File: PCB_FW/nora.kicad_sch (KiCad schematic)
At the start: 275 parts, among them J1 USB_C_Receptacle_USB2.0, J2 Conn_01x04, J3 Conn_01x02, J4 Conn_01x02, J5 Conn_02x03_Odd_Even, U1 ATmega32U4-MU, U2 24LC64, U4 Pico, Y1 16MHz

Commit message: PICOとREを接続 #89
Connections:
- net PICO_9 is gone; now on net RE1B_MOSI: J2.2 (Pin_2), U4.12 (GPIO9)
- net SCK is gone; now on net RE1A_SCK: J5.3 (Pin_3), RE_42.A, U1.9 (PB1)
- net row2: now also U4.27 (GPIO21); no longer U4.29 (GPIO22)
- net row7: now also U4.26 (GPIO20); no longer U4.27 (GPIO21)
- net MOSI renamed RE1B_MOSI
- net PICO_8 renamed RE1A_SCK
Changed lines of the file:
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@@
   (no_connect (at 358.775 62.865))
   (no_connect (at 528.32 57.785))
-  (no_connect (at 528.32 80.645))
+  (no_connect (at 528.32 73.025))
   (no_connect (at 344.17 236.22))
   (no_connect (at 528.32 70.485))
@@
     )
   )
-  (global_label "col0" (shape input) (at 492.76 52.705 180) (fields_autoplaced)
+  (global_label "RE1A_SCK" (shape input) (at 492.76 70.485 180) (fields_autoplaced)
     (effects (font (size 1.27 1.27)) (justify right))
-    (property "シート間のリファレンス" "${INTERSHEET_REFS}" (id 0) (at 0 0 0)
-      (effects (font (size 1.27 1.27)) hide)
+    (property "シート間のリファレンス" "${INTERSHEET_REFS}" (id 0) (at 481.0015 70.5644 0)
+      (effects (font (size 1.27 1.27)) (justify right) hide)
     )
   )
-  (global_label "SCK" (shape input) (at 328.295 172.72 180) (fields_autoplaced)
+  (global_label "col0" (shape input) (at 492.76 52.705 180) (fields_autoplaced)
     (effects (font (size 1.27 1.27)) (justify right))
     (property "シート間のリファレンス" "${INTERSHEET_REFS}" (id 0) (at 0 0 0)
@@
     )
   )
-  (global_label "PICO_9" (shape input) (at 492.76 73.025 180) (fields_autoplaced)
-    (effects (font (size 1.27 1.27)) (justify right))
-    (property "シート間のリファレンス" "${INTERSHEET_REFS}" (id 0) (at 0 0 0)
-      (effects (font (size 1.27 1.27)) hide)
-    )
-  )
   (global_label "Skip_R3RE" (shape input) (at 99.06 192.405 0) (fields_autoplaced)
     (effects (font (size 1.27 1.27)) (justify left))
@@
     )
   )
+  (global_label "RE1A_SCK" (shape input) (at 253.365 276.225 0) (fields_autoplaced)
+    (effects (font (size 1.27 1.27)) (justify left))
+    (property "シート間のリファレンス" "${INTERSHEET_REFS}" (id 0) (at 265.1235 276.1456 0)
+      (effects (font (size 1.27 1.27)) (justify left) hide)
+    )
+  )
   (global_label "RE1_S1" (shape input) (at 113.03 273.05 0) (fields_autoplaced)
     (effects (font (size 1.27 1.27)) (justify left))
@@
     )
   )
-  (global_label "row2" (shape input) (at 528.32 73.025 0) (fields_autoplaced)
+  (global_label "row2" (shape input) (at 528.32 78.105 0) (fields_autoplaced)
     (effects (font (size 1.27 1.27)) (justify left))
-    (property "シート間のリファレンス" "${INTERSHEET_REFS}" (id 0) (at 0 0 0)
+    (property "シート間のリファレンス" "${INTERSHEET_REFS}" (id 0) (at 0 5.08 0)
       (effects (font (size 1.27 1.27)) hide)
     )
   )
-  (global_label "PICO_8" (shape input) (at 253.365 276.225 0) (fields_autoplaced)
-    (effects (font (size 1.27 1.27)) (justify left))
-    (property "シート間のリファレンス" "${INTERSHEET_REFS}" (id 0) (at 0 0 0)
-      (effects (font (size 1.27 1.27)) hide)
+  (global_label "RE1B_MOSI" (shape input) (at 492.76 73.025 180) (fields_autoplaced)
+    (effects (font (size 1.27 1.27)) (justify right))
+    (property "シート間のリファレンス" "${INTERSHEET_REFS}" (id 0) (at 479.9734 73.1044 0)
+      (effects (font (size 1.27 1.27)) (justify right) hide)
     )
   )
@@
     )
   )
-  (global_label "MOSI" (shape input) (at 97.79 278.13 180) (fields_autoplaced)
+  (global_label "RE1B_MOSI" (shape input) (at 97.79 278.13 180) (fields_autoplaced)
     (effects (font (size 1.27 1.27)) (justify right))
-    (property "シート間のリファレンス" "${INTERSHEET_REFS}" (id 0) (at 487.045 330.835 0)
-      (effects (font (size 1.27 1.27)) hide)
+    (property "シート間のリファレンス" "${INTERSHEET_REFS}" (id 0) (at 85.0034 278.0506 0)
+      (effects (font (size 1.27 1.27)) (justify right) hide)
     )
   )
@@
     )
   )
-  (global_label "SCK" (shape input) (at 389.255 50.165 0) (fields_autoplaced)
+  (global_label "RE1A_SCK" (shape input) (at 389.255 50.165 0) (fields_autoplaced)
     (effects (font (size 1.27 1.27)) (justify left))
-    (property "シート間のリファレンス" "${INTERSHEET_REFS}" (id 0) (at 0 0 0)
-      (effects (font (size 1.27 1.27)) hide)
+    (property "シート間のリファレンス" "${INTERSHEET_REFS}" (id 0) (at 401.0135 50.0856 0)
+      (effects (font (size 1.27 1.27)) (justify left) hide)
     )
   )
@@
     )
   )
-  (global_label "MOSI" (shape input) (at 389.255 52.705 0) (fields_autoplaced)
+  (global_label "RE1B_MOSI" (shape input) (at 389.255 52.705 0) (fields_autoplaced)
     (effects (font (size 1.27 1.27)) (justify left))
-    (property "シート間のリファレンス" "${INTERSHEET_REFS}" (id 0) (at 0 0 0)
-      (effects (font (size 1.27 1.27)) hide)
+    (property "シート間のリファレンス" "${INTERSHEET_REFS}" (id 0) (at 402.0416 52.6256 0)
+      (effects (font (size 1.27 1.27)) (justify left) hide)
     )
   )
@@
     )
   )
-  (global_label "row7" (shape input) (at 528.32 78.105 0) (fields_autoplaced)
+  (global_label "row7" (shape input) (at 528.32 80.645 0) (fields_autoplaced)
     (effects (font (size 1.27 1.27)) (justify left))
-    (property "シート間のリファレンス" "${INTERSHEET_REFS}" (id 0) (at 0 0 0)
+    (property "シート間のリファレンス" "${INTERSHEET_REFS}" (id 0) (at 0 2.54 0)
       (effects (font (size 1.27 1.27)) hide)
     )
@@
     )
   )
-  (global_label "SCK" (shape input) (at 97.79 273.05 180) (fields_autoplaced)
+  (global_label "RE1A_SCK" (shape input) (at 97.79 273.05 180) (fields_autoplaced)
     (effects (font (size 1.27 1.27)) (justify right))
-    (property "シート間のリファレンス" "${INTERSHEET_REFS}" (id 0) (at 487.045 323.215 0)
-      (effects (font (size 1.27 1.27)) hide)
+    (property "シート間のリファレンス" "${INTERSHEET_REFS}" (id 0) (at 86.0315 272.9706 0)
+      (effects (font (size 1.27 1.27)) (justify right) hide)
     )
   )
@@
     )
   )
-  (global_label "PICO_9" (shape input) (at 253.365 273.685 0) (fields_autoplaced)
+  (global_label "RE1B_MOSI" (shape input) (at 340.995 172.72 0) (fields_autoplaced)
     (effects (font (size 1.27 1.27)) (justify left))
-    (property "シート間のリファレンス" "${INTERSHEET_REFS}" (id 0) (at 0 0 0)
-      (effects (font (size 1.27 1.27)) hide)
+    (property "シート間のリファレンス" "${INTERSHEET_REFS}" (id 0) (at 353.7816 172.6406 0)
+      (effects (font (size 1.27 1.27)) (justify left) hide)
     )
   )
@@
     )
   )
+  (global_label "RE1A_SCK" (shape input) (at 328.295 172.72 180) (fields_autoplaced)
+    (effects (font (size 1.27 1.27)) (justify right))
+    (property "シート間のリファレンス" "${INTERSHEET_REFS}" (id 0) (at 316.5365 172.7994 0)
+      (effects (font (size 1.27 1.27)) (justify right) hide)
+    )
+  )
   (global_label "row5" (shape input) (at 20.32 48.26 180) (fields_autoplaced)
     (effects (font (size 1.27 1.27)) (justify right))
@@
     )
   )
-  (global_label "PICO_8" (shape input) (at 492.76 70.485 180) (fields_autoplaced)
-    (effects (font (size 1.27 1.27)) (justify right))
-    (property "シート間のリファレンス" "${INTERSHEET_REFS}" (id 0) (at 0 0 0)
-      (effects (font (size 1.27 1.27)) hide)
-    )
-  )
   (global_label "col4" (shape input) (at 389.255 121.285 0) (fields_autoplaced)
     (effects (font (size 1.27 1.27)) (justify left))
@@
     )
   )
-  (global_label "MOSI" (shape input) (at 340.995 172.72 0) (fields_autoplaced)
-    (effects (font (size 1.27 1.27)) (justify left))
-    (property "シート間のリファレンス" "${INTERSHEET_REFS}" (id 0) (at 0 0 0)
-      (effects (font (size 1.27 1.27)) hide)
-    )
-  )
   (global_label "LED" (shape input) (at 528.32 60.325 0) (fields_autoplaced)
     (effects (font (size 1.27 1.27)) (justify left))
@@
     )
   )
+  (global_label "RE1B_MOSI" (shape input) (at 253.365 273.685 0) (fields_autoplaced)
+    (effects (font (size 1.27 1.27)) (justify left))
+    (property "シート間のリファレンス" "${INTERSHEET_REFS}" (id 0) (at 266.1516 273.6056 0)
+      (effects (font (size 1.27 1.27)) (justify left) hide)
+    )
+  )

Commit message: LEDの穴サイズを縦3.2→3.0mmに変更
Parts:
- L1, L10, L11, L12, L13, L14, L15, L16, L17, L18, L19, L2, L20, L21, L22, L23, L25, L26, L27, L28, L29, L3, L30, L31, L32, L33, L34, L35, L36, L37, L4, L41, L42, L43, L44, L45, L46, L47, L48, L49, L5, L50, L51, L52, L53, L56, L57, L58, L59, L6, L60, L61, L62, L63, L64, L65, L66, L68, L69, L7, L70, L71: footprint Jones.local:YS-SK6812MINI-E_large_hole_with_small_pad -> Jones.local:YS-SK6812MINI-E_middle_hole_with_small_pad
- L24, L38, L39, L40, L54, L55, L67, L8, L9: footprint Jones.local:YS-SK6812MINI-E_large_hole_with_small_pad_reserved -> Jones.local:YS-SK6812MINI-E_middle_hole_with_small_pad_reserved

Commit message: REとFWで異なるソケットの配置をわかりやすくした #109
最下段中央REのソケット
　斜線パターン
　RE→○
R3中央REのソケット
　クロスパターン
　RE→×
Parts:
- SW_37, SW_47: footprint Keebio-Parts:Kailh-PG1350-1u-MBK-WithKeyName-Socket-1.8mm-hole-reflection-half-paint -> Keebio-Parts:Kailh-PG1350-1u-MBK-WithKeyName-Socket-1.8mm-hole-reflection-cross-paint
- SW_44: footprint Keebio-Parts:Kailh-PG1350-1.5u-MBK-WithKeyName-Socket-1.8mm-hole-reflection-frame-only -> Keebio-Parts:Kailh-PG1350-1.5u-MBK-WithKeyName-Socket-1.8mm-hole-reflection-half-paint
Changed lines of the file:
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@@
     (property "Reference" "SW_37" (id 0) (at 145.415 74.041 0))
     (property "Value" ";:" (id 1) (at 145.415 76.3524 0))
-    (property "Footprint" "Keebio-Parts:Kailh-PG1350-1u-MBK-WithKeyName-Socket-1.8mm-hole-reflection-half-paint" (id 2) (at 145.415 76.2 0)
+    (property "Footprint" "Keebio-Parts:Kailh-PG1350-1u-MBK-WithKeyName-Socket-1.8mm-hole-reflection-cross-paint" (id 2) (at 145.415 76.2 0)
       (effects (font (size 1.27 1.27)) hide)
     )
@@
     (property "Reference" "SW_47" (id 0) (at 178.435 74.041 0))
     (property "Value" "'\"" (id 1) (at 178.435 76.3524 0))
-    (property "Footprint" "Keebio-Parts:Kailh-PG1350-1u-MBK-WithKeyName-Socket-1.8mm-hole-reflection-half-paint" (id 2) (at 178.435 76.2 0)
+    (property "Footprint" "Keebio-Parts:Kailh-PG1350-1u-MBK-WithKeyName-Socket-1.8mm-hole-reflection-cross-paint" (id 2) (at 178.435 76.2 0)
       (effects (font (size 1.27 1.27)) hide)
     )
@@
     (property "Reference" "SW_44" (id 0) (at 161.925 114.681 0))
     (property "Value" "Center 1.5u" (id 1) (at 161.925 116.9924 0))
-    (property "Footprint" "Keebio-Parts:Kailh-PG1350-1.5u-MBK-WithKeyName-Socket-1.8mm-hole-reflection-frame-only" (id 2) (at 161.925 116.84 0)
+    (property "Footprint" "Keebio-Parts:Kailh-PG1350-1.5u-MBK-WithKeyName-Socket-1.8mm-hole-reflection-half-paint" (id 2) (at 161.925 116.84 0)
       (effects (font (size 1.27 1.27)) hide)
     )
@@
     )
     (path "/00000000-0000-0000-0000-000061ce966c"
-      (reference "SW_37") (unit 1) (value ";:") (footprint "Keebio-Parts:Kailh-PG1350-1u-MBK-WithKeyName-Socket-1.8mm-hole-reflection-half-paint")
+      (reference "SW_37") (unit 1) (value ";:") (footprint "Keebio-Parts:Kailh-PG1350-1u-MBK-WithKeyName-Socket-1.8mm-hole-reflection-cross-paint")
     )
     (path "/cc1d72d3-c085-42d5-b51a-f25583124fcb"
@@
     )
     (path "/a2f8a0fb-e12c-4d2c-8033-a042712e74d5"
-      (reference "SW_44") (unit 1) (value "Center 1.5u") (footprint "Keebio-Parts:Kailh-PG1350-1.5u-MBK-WithKeyName-Socket-1.8mm-hole-reflection-frame-only")
+      (reference "SW_44") (unit 1) (value "Center 1.5u") (footprint "Keebio-Parts:Kailh-PG1350-1.5u-MBK-WithKeyName-Socket-1.8mm-hole-reflection-half-paint")
     )
     (path "/00000000-0000-0000-0000-000061d01246"
@@
     )
     (path "/00000000-0000-0000-0000-000061d01276"
-      (reference "SW_47") (unit 1) (value "'\"") (footprint "Keebio-Parts:Kailh-PG1350-1u-MBK-WithKeyName-Socket-1.8mm-hole-reflection-half-paint")
+      (reference "SW_47") (unit 1) (value "'\"") (footprint "Keebio-Parts:Kailh-PG1350-1u-MBK-WithKeyName-Socket-1.8mm-hole-reflection-cross-paint")
     )
     (path "/00000000-0000-0000-0000-000061d0128e"

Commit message: C1のパーツ番号を変更 #96
同じ部品だと思うのだが、以前の番号のものはExtend Partsになっている。
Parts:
- C1: LCSC C2922480 -> C15850
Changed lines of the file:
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@@
       (effects (font (size 1.27 1.27)) hide)
     )
-    (property "LCSC" "C2922480" (id 4) (at 329.565 120.015 0)
+    (property "LCSC" "C15850" (id 4) (at 329.565 120.015 0)
       (effects (font (size 1.27 1.27)) hide)
     )

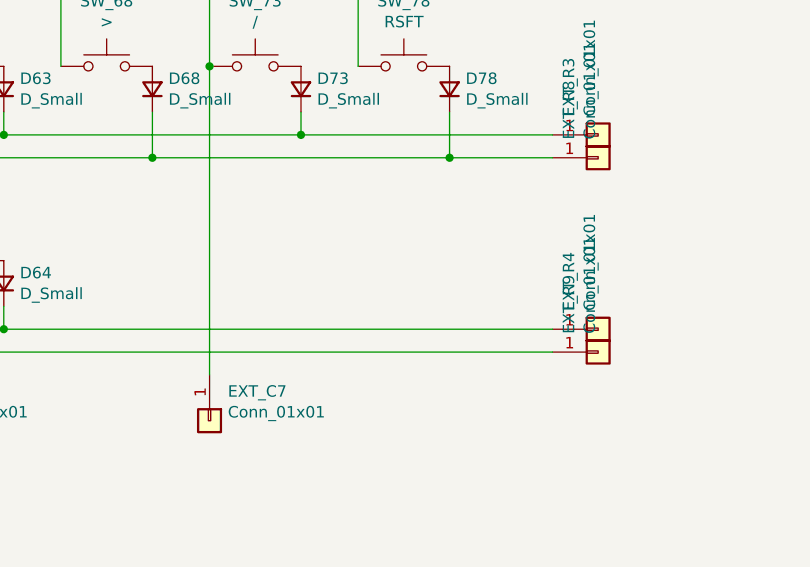
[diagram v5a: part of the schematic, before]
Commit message: エンコーダの回転をRemap/VIAで仮想機キーに割り当てるメモを追加
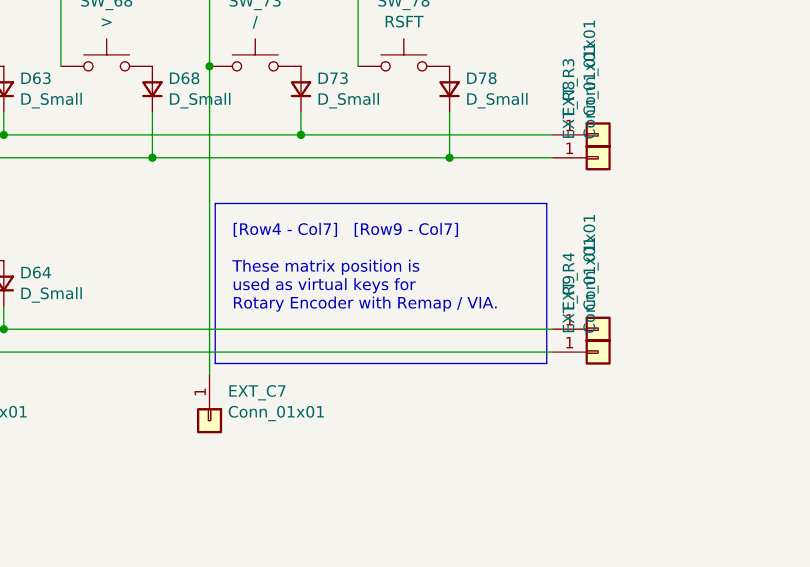
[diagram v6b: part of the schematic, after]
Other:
- note added: "[Row4 - Col7] [Row9 - Col7] These matrix position is used as virtual keys for Rotary Encoder with Remap / VIA."
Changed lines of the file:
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@@
+    (stroke (width 0) (type default) (color 0 0 0 0))
+  )
+  (polyline (pts (xy 256.54 118.11) (xy 256.54 135.89))
     (stroke (width 0) (type default) (color 0 0 0 0))
   )
@@
     (stroke (width 0) (type default) (color 0 0 0 0))
   )
+  (polyline (pts (xy 256.54 118.11) (xy 293.37 118.11))
+    (stroke (width 0) (type default) (color 0 0 0 0))
+  )
   (wire (pts (xy 335.915 122.555) (xy 335.915 125.095))
     (stroke (width 0) (type default) (color 0 0 0 0))
@@
     (stroke (width 0) (type default) (color 0 0 0 0))
   )
+  (polyline (pts (xy 293.37 135.89) (xy 256.54 135.89))
+    (stroke (width 0) (type default) (color 0 0 0 0))
+  )
   (wire (pts (xy 216.535 43.18) (xy 216.535 48.26))
     (stroke (width 0) (type default) (color 0 0 0 0))
@@
   )
   (wire (pts (xy 112.395 189.23) (xy 112.395 192.405))
+    (stroke (width 0) (type default) (color 0 0 0 0))
+  )
+  (polyline (pts (xy 293.37 118.11) (xy 293.37 135.89))
     (stroke (width 0) (type default) (color 0 0 0 0))
   )
@@
     (effects (font (size 2.54 2.54) (thickness 0.508) bold) (justify left bottom))
   )
+  (text "[Row4 - Col7]   [Row9 - Col7]\n\nThese matrix position is \nused as virtual keys for \nRotary Encoder with Remap / VIA."
+    (at 258.445 130.175 0)
+    (effects (font (size 1.27 1.27)) (justify left bottom))
+  )
   (text "SPEAKER" (at 272.415 164.465 0)

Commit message: アイコンでなんとか表現しようとしている
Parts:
- SW_35, SW_38, SW_40, SW_41, SW_42, SW_43: footprint Keebio-Parts:Kailh-PG1350-1u-MBK-WithKeyName-Socket-1.8mm-hole-reflection-frame-only -> Keebio-Parts:Kailh-PG1350-1u-MBK-WithKeyName-Socket-1.8mm-hole-reflection-no-frame
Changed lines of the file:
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@@
     (property "Reference" "SW_43" (id 0) (at 161.925 95.631 0))
     (property "Value" "R4R" (id 1) (at 161.925 97.9424 0))
-    (property "Footprint" "Keebio-Parts:Kailh-PG1350-1u-MBK-WithKeyName-Socket-1.8mm-hole-reflection-frame-only" (id 2) (at 161.925 97.79 0)
+    (property "Footprint" "Keebio-Parts:Kailh-PG1350-1u-MBK-WithKeyName-Socket-1.8mm-hole-reflection-no-frame" (id 2) (at 161.925 97.79 0)
       (effects (font (size 1.27 1.27)) hide)
     )
@@
     (property "Reference" "SW_40" (id 0) (at 161.925 30.861 0))
     (property "Value" "R1R" (id 1) (at 161.925 33.1724 0))
-    (property "Footprint" "Keebio-Parts:Kailh-PG1350-1u-MBK-WithKeyName-Socket-1.8mm-hole-reflection-frame-only" (id 2) (at 161.925 33.02 0)
+    (property "Footprint" "Keebio-Parts:Kailh-PG1350-1u-MBK-WithKeyName-Socket-1.8mm-hole-reflection-no-frame" (id 2) (at 161.925 33.02 0)
       (effects (font (size 1.27 1.27)) hide)
     )
@@
     (property "Reference" "SW_42" (id 0) (at 161.925 74.041 0))
     (property "Value" "R3C" (id 1) (at 161.925 76.3524 0))
-    (property "Footprint" "Keebio-Parts:Kailh-PG1350-1u-MBK-WithKeyName-Socket-1.8mm-hole-reflection-frame-only" (id 2) (at 161.925 76.2 0)
+    (property "Footprint" "Keebio-Parts:Kailh-PG1350-1u-MBK-WithKeyName-Socket-1.8mm-hole-reflection-no-frame" (id 2) (at 161.925 76.2 0)
       (effects (font (size 1.27 1.27)) hide)
     )
@@
     (property "Reference" "SW_38" (id 0) (at 145.415 95.631 0))
     (property "Value" "R4L" (id 1) (at 145.415 97.9424 0))
-    (property "Footprint" "Keebio-Parts:Kailh-PG1350-1u-MBK-WithKeyName-Socket-1.8mm-hole-reflection-frame-only" (id 2) (at 145.415 97.79 0)
+    (property "Footprint" "Keebio-Parts:Kailh-PG1350-1u-MBK-WithKeyName-Socket-1.8mm-hole-reflection-no-frame" (id 2) (at 145.415 97.79 0)
       (effects (font (size 1.27 1.27)) hide)
     )
@@
     (property "Reference" "SW_41" (id 0) (at 161.925 52.451 0))
     (property "Value" "R2C" (id 1) (at 161.925 54.7624 0))
-    (property "Footprint" "Keebio-Parts:Kailh-PG1350-1u-MBK-WithKeyName-Socket-1.8mm-hole-reflection-frame-only" (id 2) (at 161.925 54.61 0)
+    (property "Footprint" "Keebio-Parts:Kailh-PG1350-1u-MBK-WithKeyName-Socket-1.8mm-hole-reflection-no-frame" (id 2) (at 161.925 54.61 0)
       (effects (font (size 1.27 1.27)) hide)
     )
@@
     (property "Reference" "SW_35" (id 0) (at 145.415 30.861 0))
     (property "Value" "R1L" (id 1) (at 145.415 33.1724 0))
-    (property "Footprint" "Keebio-Parts:Kailh-PG1350-1u-MBK-WithKeyName-Socket-1.8mm-hole-reflection-frame-only" (id 2) (at 145.415 33.02 0)
+    (property "Footprint" "Keebio-Parts:Kailh-PG1350-1u-MBK-WithKeyName-Socket-1.8mm-hole-reflection-no-frame" (id 2) (at 145.415 33.02 0)
       (effects (font (size 1.27 1.27)) hide)
     )
@@
     )
     (path "/efce3ccf-dccf-4ab2-825c-383d2306383e"
-      (reference "SW_35") (unit 1) (value "R1L") (footprint "Keebio-Parts:Kailh-PG1350-1u-MBK-WithKeyName-Socket-1.8mm-hole-reflection-frame-only")
+      (reference "SW_35") (unit 1) (value "R1L") (footprint "Keebio-Parts:Kailh-PG1350-1u-MBK-WithKeyName-Socket-1.8mm-hole-reflection-no-frame")
     )
     (path "/00000000-0000-0000-0000-000061ce9654"
@@
     )
     (path "/cc1d72d3-c085-42d5-b51a-f25583124fcb"
-      (reference "SW_38") (unit 1) (value "R4L") (footprint "Keebio-Parts:Kailh-PG1350-1u-MBK-WithKeyName-Socket-1.8mm-hole-reflection-frame-only")
+      (reference "SW_38") (unit 1) (value "R4L") (footprint "Keebio-Parts:Kailh-PG1350-1u-MBK-WithKeyName-Socket-1.8mm-hole-reflection-no-frame")
     )
     (path "/00000000-0000-0000-0000-000061ce969c"
@@
     )
     (path "/164abd3f-e22c-4c79-a335-ba856dad611c"
-      (reference "SW_40") (unit 1) (value "R1R") (footprint "Keebio-Parts:Kailh-PG1350-1u-MBK-WithKeyName-Socket-1.8mm-hole-reflection-frame-only")
+      (reference "SW_40") (unit 1) (value "R1R") (footprint "Keebio-Parts:Kailh-PG1350-1u-MBK-WithKeyName-Socket-1.8mm-hole-reflection-no-frame")
     )
     (path "/ef3363f5-8d79-4ecf-984c-7cb0bf9cde9e"
-      (reference "SW_41") (unit 1) (value "R2C") (footprint "Keebio-Parts:Kailh-PG1350-1u-MBK-WithKeyName-Socket-1.8mm-hole-reflection-frame-only")
+      (reference "SW_41") (unit 1) (value "R2C") (footprint "Keebio-Parts:Kailh-PG1350-1u-MBK-WithKeyName-Socket-1.8mm-hole-reflection-no-frame")
     )
     (path "/8f0205a6-0769-462f-bc35-3f1d10f4a746"
-      (reference "SW_42") (unit 1) (value "R3C") (footprint "Keebio-Parts:Kailh-PG1350-1u-MBK-WithKeyName-Socket-1.8mm-hole-reflection-frame-only")
+      (reference "SW_42") (unit 1) (value "R3C") (footprint "Keebio-Parts:Kailh-PG1350-1u-MBK-WithKeyName-Socket-1.8mm-hole-reflection-no-frame")
     )
     (path "/0dea41fa-0c6a-48a7-81ed-660971009e1c"
-      (reference "SW_43") (unit 1) (value "R4R") (footprint "Keebio-Parts:Kailh-PG1350-1u-MBK-WithKeyName-Socket-1.8mm-hole-reflection-frame-only")
+      (reference "SW_43") (unit 1) (value "R4R") (footprint "Keebio-Parts:Kailh-PG1350-1u-MBK-WithKeyName-Socket-1.8mm-hole-reflection-no-frame")
     )
     (path "/a2f8a0fb-e12c-4d2c-8033-a042712e74d5"

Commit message: 最下行中央のキーをREから外す
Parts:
- SW_44: footprint Keebio-Parts:Kailh-PG1350-1.5u-MBK-WithKeyName-Socket-1.8mm-hole-reflection-half-paint -> Keebio-Parts:Kailh-PG1350-1.5u-MBK-WithKeyName-Socket-1.8mm-hole-reflection-frame-only
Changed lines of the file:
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@@
     (property "Reference" "SW_44" (id 0) (at 161.925 114.681 0))
     (property "Value" "Center 1.5u" (id 1) (at 161.925 116.9924 0))
-    (property "Footprint" "Keebio-Parts:Kailh-PG1350-1.5u-MBK-WithKeyName-Socket-1.8mm-hole-reflection-half-paint" (id 2) (at 161.925 116.84 0)
+    (property "Footprint" "Keebio-Parts:Kailh-PG1350-1.5u-MBK-WithKeyName-Socket-1.8mm-hole-reflection-frame-only" (id 2) (at 161.925 116.84 0)
       (effects (font (size 1.27 1.27)) hide)
     )
@@
     )
     (path "/a2f8a0fb-e12c-4d2c-8033-a042712e74d5"
-      (reference "SW_44") (unit 1) (value "Center 1.5u") (footprint "Keebio-Parts:Kailh-PG1350-1.5u-MBK-WithKeyName-Socket-1.8mm-hole-reflection-half-paint")
+      (reference "SW_44") (unit 1) (value "Center 1.5u") (footprint "Keebio-Parts:Kailh-PG1350-1.5u-MBK-WithKeyName-Socket-1.8mm-hole-reflection-frame-only")
     )
     (path "/00000000-0000-0000-0000-000061d01246"
